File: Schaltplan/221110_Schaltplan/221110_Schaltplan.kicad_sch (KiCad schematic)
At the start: 21 parts, among them J0 LDR0/Vsolar, J1 LDR1, J10 LDR2, J11 LDR3, J2 LDR2, J3 LDR3, J4 Dspl SDA, J5 Dspl SCL, J6 Srv0, J7 Srv1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

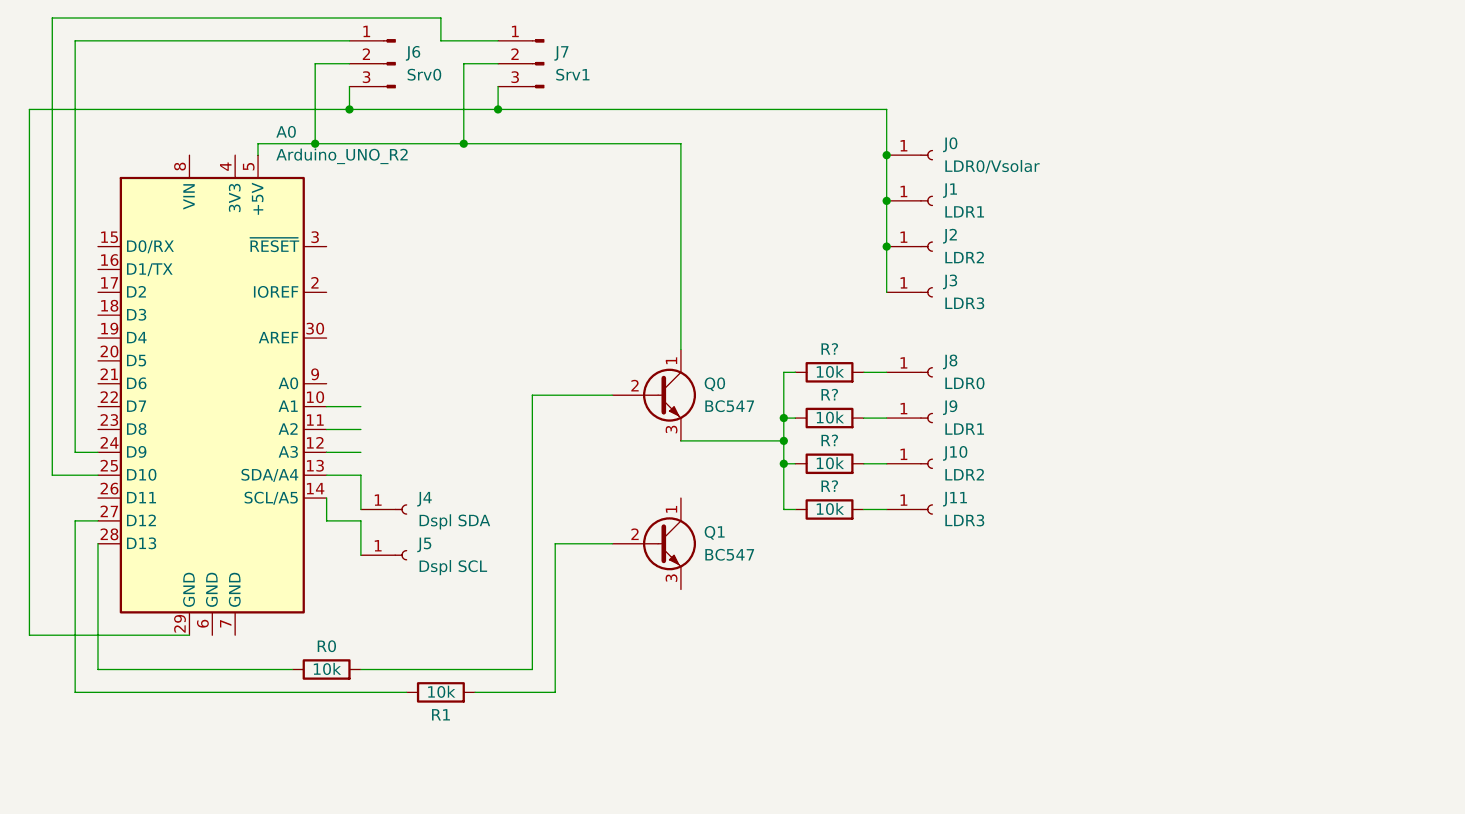
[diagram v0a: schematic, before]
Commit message: Add ADC to Curcuit Diagram
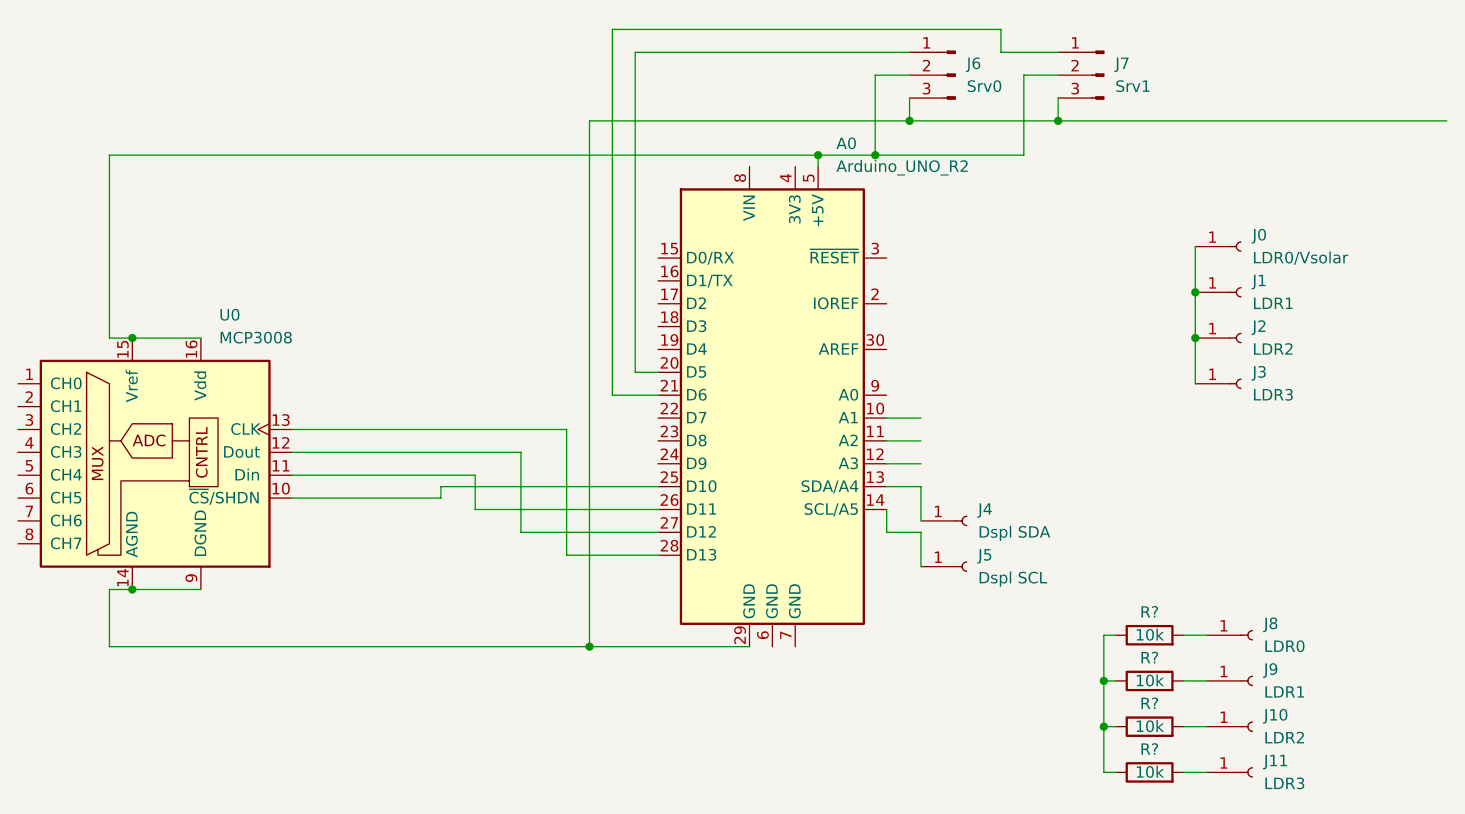
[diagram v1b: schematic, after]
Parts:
- removed Q0, Q1: BC547, Package_TO_SOT_THT:TO-92_Inline, symbol Transistor_BJT:BC547
- removed R0, R1: 10k, symbol Device:R
- added U0: MCP3008, symbol Analog_ADC:MCP3008
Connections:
- net at J6.1 (Pin_1): now also A0.20 (D5); no longer A0.24 (D9)
- net at A0.5 (+5V), J6.2 (Pin_2), J7.2 (Pin_2): now also U0.15 (Vref), U0.16 (Vdd)
- net at J0.1 (Pin_1), J1.1 (Pin_1), J2.1 (Pin_1)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: no longer A0.29 (GND), J6.3 (Pin_3), J7.3 (Pin_3)
- net at A0.28 (D13): now also U0.13 (CLK)
- net at A0.25 (D10): now also U0.10 (~{CS}/SHDN); no longer J7.1 (Pin_1)
- net at A0.21 (D6): now also J7.1 (Pin_1)
- net at A0.26 (D11): now also U0.11 (Din)
- net at A0.27 (D12): now also U0.12 (Dout)
- new net: A0.29 (GND), J6.3 (Pin_3), J7.3 (Pin_3), U0.14 (AGND), U0.9 (DGND)
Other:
- moved on the sheet: A0, J0, J1, J10, J11, J2, J3, J4, J5, J6, J7, J8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
